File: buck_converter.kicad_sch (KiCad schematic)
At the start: 18 parts, among them U3 LMR604403SRAKR, U4 LMR604403SRAKR

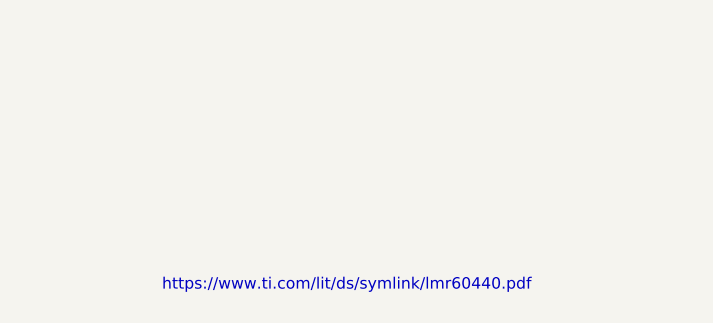
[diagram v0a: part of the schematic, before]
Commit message: new mounting holes
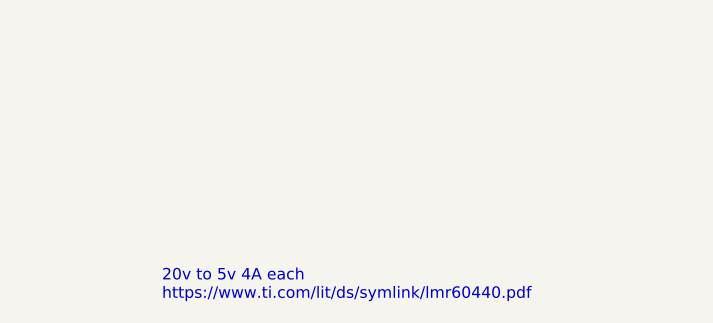
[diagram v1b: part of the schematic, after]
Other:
- note added: "20v to 5v 4A each https://www.ti.com/lit/ds/symlink/lmr60440.pdf"
- note removed: "https://www.ti.com/lit/ds/symlink/lmr60440.pdf"
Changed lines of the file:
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@@
 	(generator_version "9.0")
 	(paper "A4")
-	(text "https://www.ti.com/lit/ds/symlink/lmr60440.pdf"
+	(text "20v to 5v 4A each\nhttps://www.ti.com/lit/ds/symlink/lmr60440.pdf"
 		(exclude_from_sim no)
 		(at 178.562 169.164 0)

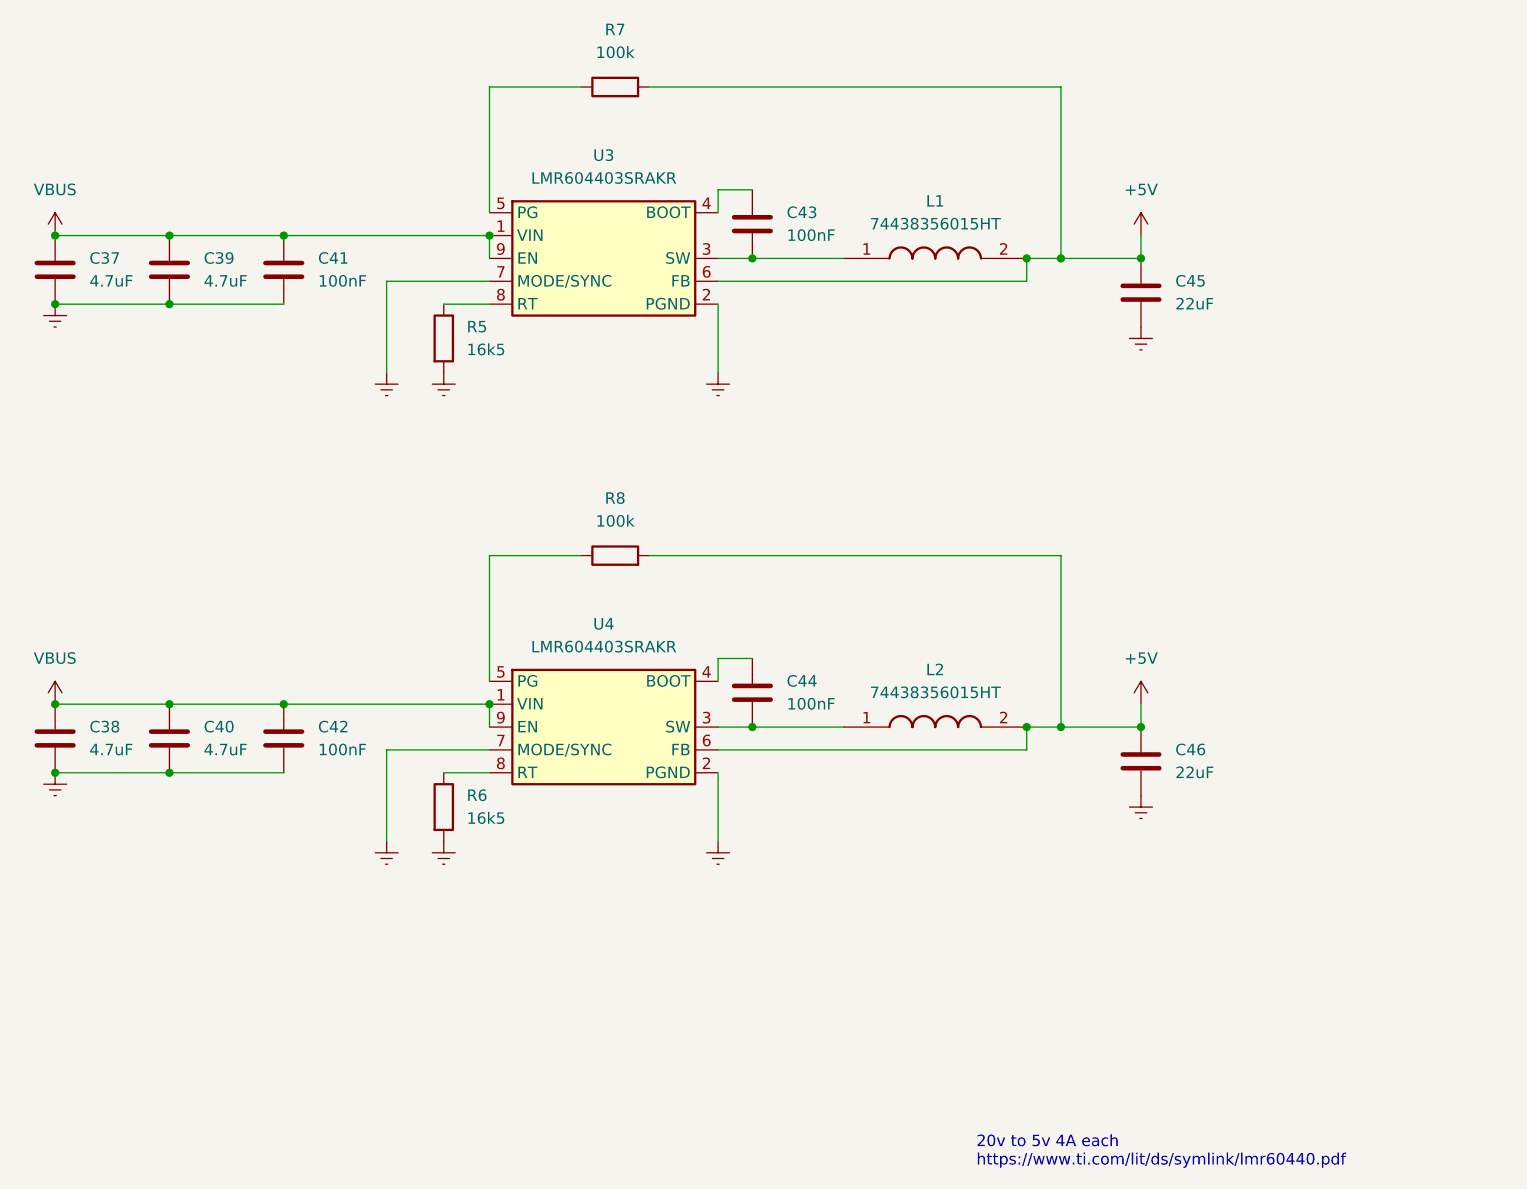
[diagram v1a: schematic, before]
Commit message: buck converter test pads and optional resistors
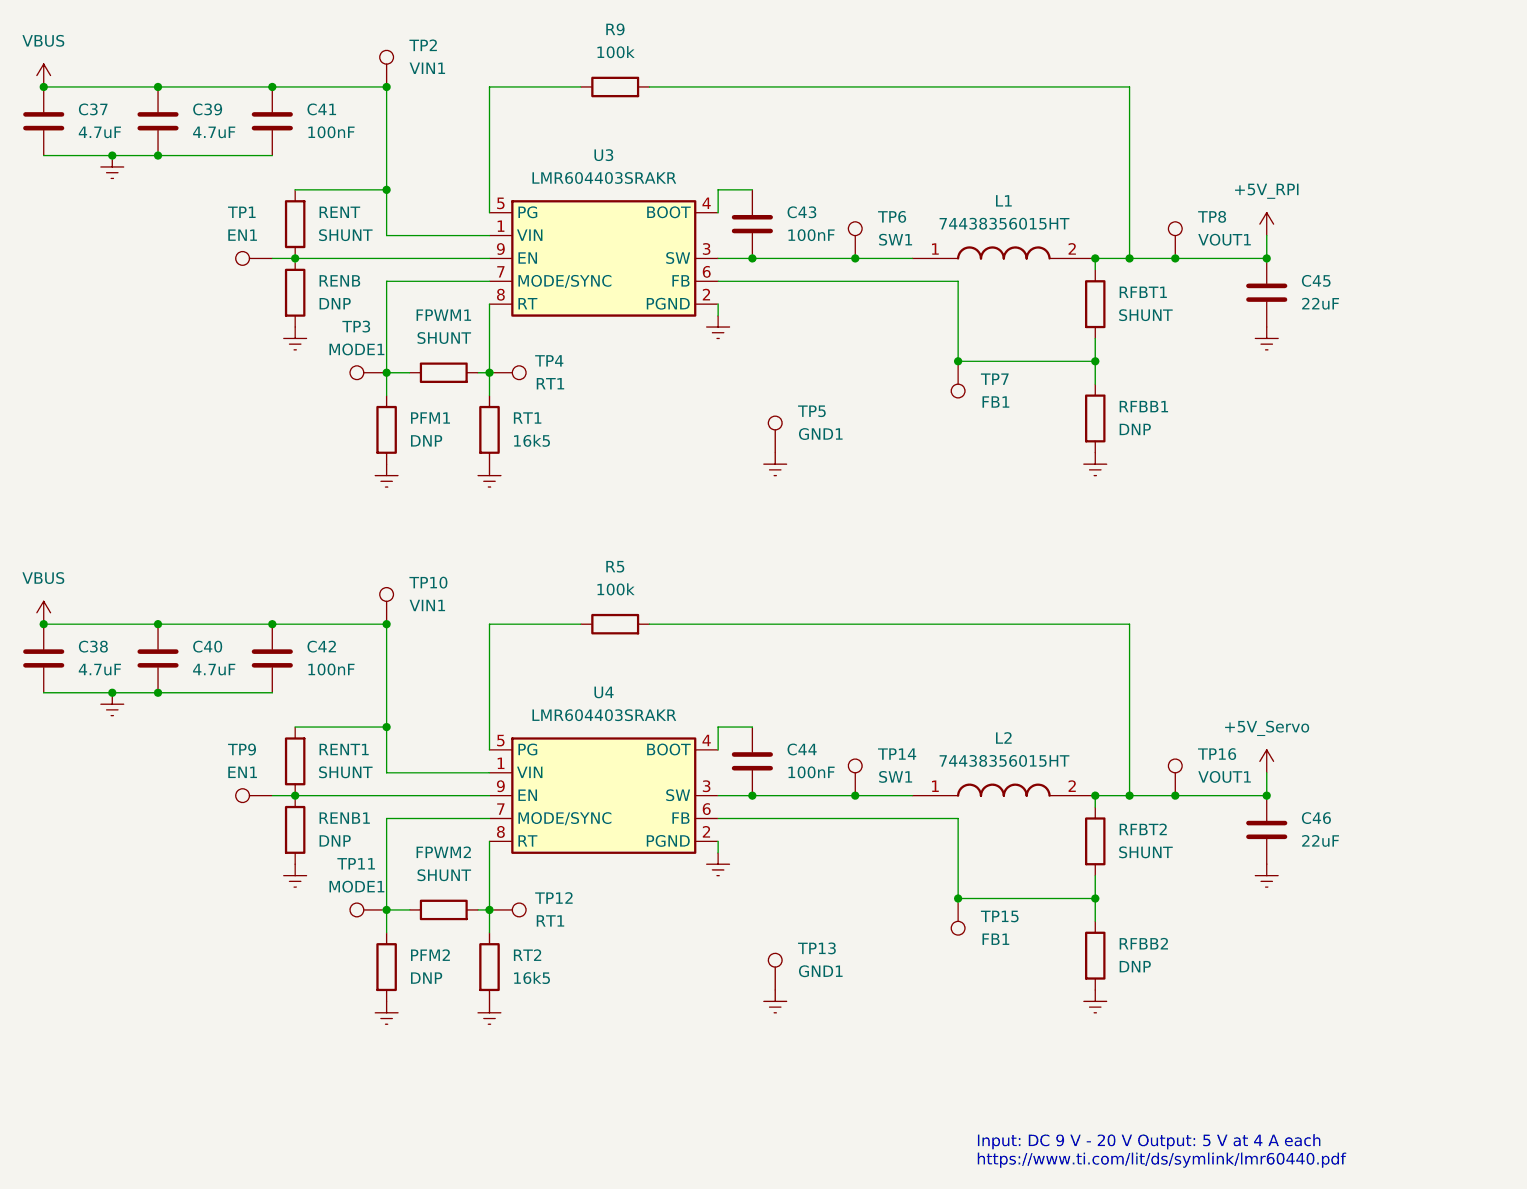
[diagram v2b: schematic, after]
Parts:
- removed R6: 16k5, Resistor_SMD:R_0603_1608Metric_Pad0.98x0.95mm_HandSolder, symbol Device:R
- removed R8: 100k, Resistor_SMD:R_0603_1608Metric_Pad0.98x0.95mm_HandSolder, symbol Device:R
- added FPWM1, FPWM2, RENT, RENT1, RFBT1, RFBT2: SHUNT, Resistor_SMD:R_0603_1608Metric_Pad0.98x0.95mm_HandSolder, symbol Device:R
- added PFM1, PFM2, RENB, RENB1, RFBB1, RFBB2: DNP, Resistor_SMD:R_0603_1608Metric_Pad0.98x0.95mm_HandSolder, symbol Device:R
- added R5: 100k, Resistor_SMD:R_0603_1608Metric_Pad0.98x0.95mm_HandSolder, symbol Device:R
- added RT2: 16k5, Resistor_SMD:R_0603_1608Metric_Pad0.98x0.95mm_HandSolder, symbol Device:R
- added TP1, TP9: EN1, TestPoint:TestPoint_Pad_D2.0mm, symbol Connector:TestPoint
- added TP10, TP2: VIN1, TestPoint:TestPoint_Pad_D2.0mm, symbol Connector:TestPoint
- added TP11, TP3: MODE1, TestPoint:TestPoint_Pad_D2.0mm, symbol Connector:TestPoint
- added TP12, TP4: RT1, TestPoint:TestPoint_Pad_D2.0mm, symbol Connector:TestPoint
- added TP13, TP5: GND1, TestPoint:TestPoint_Pad_D2.0mm, symbol Connector:TestPoint
- added TP14, TP6: SW1, TestPoint:TestPoint_Pad_D2.0mm, symbol Connector:TestPoint
- added TP15, TP7: FB1, TestPoint:TestPoint_Pad_D2.0mm, symbol Connector:TestPoint
- added TP16, TP8: VOUT1, TestPoint:TestPoint_Pad_D2.0mm, symbol Connector:TestPoint
- renumbered R7 to R9, R5 to RT1
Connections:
- net GND: now also PFM1.2, PFM2.2, RENB.2, RENB1.2, RFBB1.2, RFBB2.2, RT2.2, TP13.1, TP5.1; no longer U3.7 (MODE/SYNC), U4.7 (MODE/SYNC)
- net VBUS: now also RENT.2, RENT1.2, TP10.1, TP2.1; no longer U3.9 (EN), U4.9 (EN)
- net at C43.2, L1.1, U3.3 (SW): now also TP6.1
- net at C44.2, L2.1, U4.3 (SW): now also TP14.1
- net at U4.5 (PG): now also R5.1
- net at U4.8 (RT): now also FPWM2.2, RT2.1, TP12.1
- net at RT1.1, U3.8 (RT): now also FPWM1.2, TP4.1
- removed net +5V: C45.1, C46.1, L1.2, L2.2, R9.2, U3.6 (FB), U4.6 (FB)
- new net: RFBB1.1, RFBT1.2, TP7.1, U3.6 (FB)
- new net: RFBB2.1, RFBT2.2, TP15.1, U4.6 (FB)
- new net: FPWM2.1, PFM2.1, TP11.1, U4.7 (MODE/SYNC)
- new net: RENB.1, RENT.1, TP1.1, U3.9 (EN)
- new net: FPWM1.1, PFM1.1, TP3.1, U3.7 (MODE/SYNC)
- new net: RENB1.1, RENT1.1, TP9.1, U4.9 (EN)
- new net +5V_RPI: C45.1, L1.2, R9.2, RFBT1.1, TP8.1
- new net +5V_Servo: C46.1, L2.2, R5.2, RFBT2.1, TP16.1
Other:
- note added: "Input: DC 9 V - 20 V Output: 5 V at 4 A each https://www.ti.com/lit/ds/symlink/lmr60440.pdf"
- note removed: "20v to 5v 4A each https://www.ti.com/lit/ds/symlink/lmr60440.pdf"
- moved on the sheet: C37, C39, C41, C45, L1, RT1

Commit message: some footprint for LMR60440
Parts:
- U3, U4: footprint (none) -> Package_DFN_QFN:LMR60440
- renumbered R9 to R5, R5 to R6, RENB to RENB1, RENB1 to RENB2, RENT to RENT1, RENT1 to RENT2, TP13 to TP10, TP6 to TP11, TP14 to TP12, TP7 to TP13, TP15 to TP14, TP8 to TP15, TP9 to TP2, TP2 to TP3, TP3 to TP4, TP10 to TP5, TP11 to TP6, TP4 to TP7, TP12 to TP8, TP5 to TP9

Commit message: bit of layout. new LMR60440 footprint
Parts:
- U3, U4: footprint Package_DFN_QFN:LMR60440 -> KiCad:QFN-9_2.5x2.0mm_RAK
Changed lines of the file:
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@@
 			)
 		)
-		(property "Footprint" "Package_DFN_QFN:LMR60440"
+		(property "Footprint" "KiCad:QFN-9_2.5x2.0mm_RAK"
 			(at 132.08 63.5 0)
 			(effects
@@
 			)
 		)
-		(property "Footprint" "Package_DFN_QFN:LMR60440"
+		(property "Footprint" "KiCad:QFN-9_2.5x2.0mm_RAK"
 			(at 132.08 123.19 0)
 			(effects

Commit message: smaller test pads. some routing
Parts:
- TP1, TP10, TP11, TP12, TP13, TP14, TP15, TP16, TP2, TP3, TP4, TP5, TP6, TP7, TP8, TP9: footprint TestPoint:TestPoint_Pad_D2.0mm -> TestPoint:TestPoint_Pad_D1.0mm
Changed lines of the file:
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@@
 			)
 		)
-		(property "Footprint" "TestPoint:TestPoint_Pad_D2.0mm"
+		(property "Footprint" "TestPoint:TestPoint_Pad_D1.0mm"
 			(at 205.74 69.85 0)
 			(effects
@@
 			)
 		)
-		(property "Footprint" "TestPoint:TestPoint_Pad_D2.0mm"
+		(property "Footprint" "TestPoint:TestPoint_Pad_D1.0mm"
 			(at 161.29 151.13 0)
 			(effects
@@
 			)
 		)
-		(property "Footprint" "TestPoint:TestPoint_Pad_D2.0mm"
+		(property "Footprint" "TestPoint:TestPoint_Pad_D1.0mm"
 			(at 124.46 147.32 0)
 			(effects
@@
 			)
 		)
-		(property "Footprint" "TestPoint:TestPoint_Pad_D2.0mm"
+		(property "Footprint" "TestPoint:TestPoint_Pad_D1.0mm"
 			(at 113.03 137.16 0)
 			(effects
@@
 			)
 		)
-		(property "Footprint" "TestPoint:TestPoint_Pad_D2.0mm"
+		(property "Footprint" "TestPoint:TestPoint_Pad_D1.0mm"
 			(at 100.33 64.77 0)
 			(effects
@@
 			)
 		)
-		(property "Footprint" "TestPoint:TestPoint_Pad_D2.0mm"
+		(property "Footprint" "TestPoint:TestPoint_Pad_D1.0mm"
 			(at 170.18 129.54 0)
 			(effects
@@
 			)
 		)
-		(property "Footprint" "TestPoint:TestPoint_Pad_D2.0mm"
+		(property "Footprint" "TestPoint:TestPoint_Pad_D1.0mm"
 			(at 100.33 124.46 0)
 			(effects
@@
 			)
 		)
-		(property "Footprint" "TestPoint:TestPoint_Pad_D2.0mm"
+		(property "Footprint" "TestPoint:TestPoint_Pad_D1.0mm"
 			(at 171.45 81.28 0)
 			(effects
@@
 			)
 		)
-		(property "Footprint" "TestPoint:TestPoint_Pad_D2.0mm"
+		(property "Footprint" "TestPoint:TestPoint_Pad_D1.0mm"
 			(at 118.11 50.8 0)
 			(effects
@@
 			)
 		)
-		(property "Footprint" "TestPoint:TestPoint_Pad_D2.0mm"
+		(property "Footprint" "TestPoint:TestPoint_Pad_D1.0mm"
 			(at 113.03 77.47 0)
 			(effects
@@
 			)
 		)
-		(property "Footprint" "TestPoint:TestPoint_Pad_D2.0mm"
+		(property "Footprint" "TestPoint:TestPoint_Pad_D1.0mm"
 			(at 124.46 87.63 0)
 			(effects
@@
 			)
 		)
-		(property "Footprint" "TestPoint:TestPoint_Pad_D2.0mm"
+		(property "Footprint" "TestPoint:TestPoint_Pad_D1.0mm"
 			(at 170.18 69.85 0)
 			(effects
@@
 			)
 		)
-		(property "Footprint" "TestPoint:TestPoint_Pad_D2.0mm"
+		(property "Footprint" "TestPoint:TestPoint_Pad_D1.0mm"
 			(at 118.11 110.49 0)
 			(effects
@@
 			)
 		)
-		(property "Footprint" "TestPoint:TestPoint_Pad_D2.0mm"
+		(property "Footprint" "TestPoint:TestPoint_Pad_D1.0mm"
 			(at 205.74 129.54 0)
 			(effects
@@
 			)
 		)
-		(property "Footprint" "TestPoint:TestPoint_Pad_D2.0mm"
+		(property "Footprint" "TestPoint:TestPoint_Pad_D1.0mm"
 			(at 171.45 140.97 0)
 			(effects
@@
 			)
 		)
-		(property "Footprint" "TestPoint:TestPoint_Pad_D2.0mm"
+		(property "Footprint" "TestPoint:TestPoint_Pad_D1.0mm"
 			(at 161.29 91.44 0)
 			(effects

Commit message: silkscreen: logo, text, testpads.
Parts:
- TP10: value GND1 -> GND2
- TP12: value SW1 -> SW2
- TP14: value FB1 -> FB2
- TP16: value VOUT1 -> VOUT2
- TP2: value EN1 -> EN2
- TP5: value VIN1 -> VIN2
- TP6: value MODE1 -> MODE2
- TP8: value RT1 -> RT2
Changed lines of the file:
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@@
 			)
 		)
-		(property "Value" "GND1"
+		(property "Value" "GND2"
 			(at 158.75 149.0979 0)
 			(effects
@@
 			)
 		)
-		(property "Value" "RT1"
+		(property "Value" "RT2"
 			(at 129.54 143.5099 90)
 			(effects
@@
 			)
 		)
-		(property "Value" "MODE1"
+		(property "Value" "MODE2"
 			(at 109.728 139.7 90)
 			(effects
@@
 			)
 		)
-		(property "Value" "SW1"
+		(property "Value" "SW2"
 			(at 167.64 127.5079 0)
 			(effects
@@
 			)
 		)
-		(property "Value" "EN1"
+		(property "Value" "EN2"
 			(at 97.028 127 90)
 			(effects
@@
 			)
 		)
-		(property "Value" "VIN1"
+		(property "Value" "VIN2"
 			(at 115.57 108.4579 0)
 			(effects
@@
 			)
 		)
-		(property "Value" "VOUT1"
+		(property "Value" "VOUT2"
 			(at 203.2 127.5079 0)
 			(effects
@@
 			)
 		)
-		(property "Value" "FB1"
+		(property "Value" "FB2"
 			(at 179.07 145.5419 0)
 			(effects

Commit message: generic 2.54mm headers and testPads excluded from BOM
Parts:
- PFM1, PFM2, RENB1, RENB2, RFBB1, RFBB2: now not fitted
- TP1, TP10, TP11, TP12, TP13, TP14, TP15, TP16, TP2, TP3, TP4, TP5, TP6, TP7, TP8, TP9: now left out of the parts list
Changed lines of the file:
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@@
 		(unit 1)
 		(exclude_from_sim no)
-		(in_bom yes)
+		(in_bom no)
 		(on_board yes)
 		(dnp no)
@@
 		(unit 1)
 		(exclude_from_sim no)
-		(in_bom yes)
+		(in_bom no)
 		(on_board yes)
 		(dnp no)
@@
 		(in_bom yes)
 		(on_board yes)
-		(dnp no)
+		(dnp yes)
 		(fields_autoplaced yes)
 		(property "Reference" "RFBB2"
@@
 		(unit 1)
 		(exclude_from_sim no)
-		(in_bom yes)
+		(in_bom no)
 		(on_board yes)
 		(dnp no)
@@
 		(unit 1)
 		(exclude_from_sim no)
-		(in_bom yes)
+		(in_bom no)
 		(on_board yes)
 		(dnp no)
@@
 		(unit 1)
 		(exclude_from_sim no)
-		(in_bom yes)
+		(in_bom no)
 		(on_board yes)
 		(dnp no)
@@
 		(unit 1)
 		(exclude_from_sim no)
-		(in_bom yes)
+		(in_bom no)
 		(on_board yes)
 		(dnp no)
@@
 		(unit 1)
 		(exclude_from_sim no)
-		(in_bom yes)
+		(in_bom no)
 		(on_board yes)
 		(dnp no)
@@
 		(in_bom yes)
 		(on_board yes)
-		(dnp no)
+		(dnp yes)
 		(fields_autoplaced yes)
 		(property "Reference" "PFM2"
@@
 		(unit 1)
 		(exclude_from_sim no)
-		(in_bom yes)
+		(in_bom no)
 		(on_board yes)
 		(dnp no)
@@
 		(in_bom yes)
 		(on_board yes)
-		(dnp no)
+		(dnp yes)
 		(fields_autoplaced yes)
 		(property "Reference" "RENB1"
@@
 		(unit 1)
 		(exclude_from_sim no)
-		(in_bom yes)
+		(in_bom no)
 		(on_board yes)
 		(dnp no)
@@
 		(in_bom yes)
 		(on_board yes)
-		(dnp no)
+		(dnp yes)
 		(fields_autoplaced yes)
 		(property "Reference" "RENB2"
@@
 		(unit 1)
 		(exclude_from_sim no)
-		(in_bom yes)
+		(in_bom no)
 		(on_board yes)
 		(dnp no)
@@
 		(unit 1)
 		(exclude_from_sim no)
-		(in_bom yes)
+		(in_bom no)
 		(on_board yes)
 		(dnp no)
@@
 		(unit 1)
 		(exclude_from_sim no)
-		(in_bom yes)
+		(in_bom no)
 		(on_board yes)
 		(dnp no)
@@
 		(in_bom yes)
 		(on_board yes)
-		(dnp no)
+		(dnp yes)
 		(fields_autoplaced yes)
 		(property "Reference" "PFM1"
@@
 		(in_bom yes)
 		(on_board yes)
-		(dnp no)
+		(dnp yes)
 		(fields_autoplaced yes)
 		(property "Reference" "RFBB1"
@@
 		(unit 1)
 		(exclude_from_sim no)
-		(in_bom yes)
+		(in_bom no)
 		(on_board yes)
 		(dnp no)
@@
 		(unit 1)
 		(exclude_from_sim no)
-		(in_bom yes)
+		(in_bom no)
 		(on_board yes)
 		(dnp no)
@@
 		(unit 1)
 		(exclude_from_sim no)
-		(in_bom yes)
+		(in_bom no)
 		(on_board yes)
 		(dnp no)
@@
 		(unit 1)
 		(exclude_from_sim no)
-		(in_bom yes)
+		(in_bom no)
 		(on_board yes)
 		(dnp no)
